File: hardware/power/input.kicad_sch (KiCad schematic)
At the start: 26 parts, among them J101 24V IN, Q101 SQJ457EP, Q102 SQJ457EP, SW101 POWER, U101 L78M05, U102 74HC14

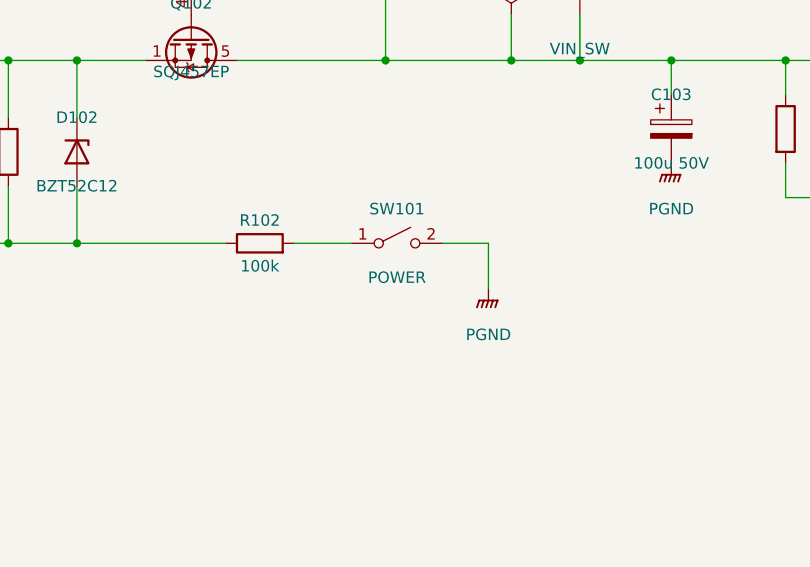
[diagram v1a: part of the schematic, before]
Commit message: Power board: E24 dividers, rear-panel rocker, last parts chosen (decisions 156-159)
- 156: UVLO 680k/39k (start 21.3 V, stop 19.0 V), RT 240k, buck
  compensation 16k; design.py and startup_sim.py rerun (start-up unchanged,
  GSM220B24 limit in the model)
- 157: power switch a Legion SS11-BBIWG-R20-R rocker on the rear panel,
  wired to J102 (JST XH 2-pin) in place of SW101; counted in costs.py
- 158: C103 Nichicon UHE1H101MPD radial; sync caps 10 pF C0G 50 V 0603
- 159: D201 SS54 on D_SMA to match LCSC C22452
- Netlist checks 0 problems, ERC 0/0; estimate 764/1045/1641 EUR
  (4/8/16 ch), 28 fee types

Co-Authored-By: Claude Opus 5.5 <noreply@anthropic.com>
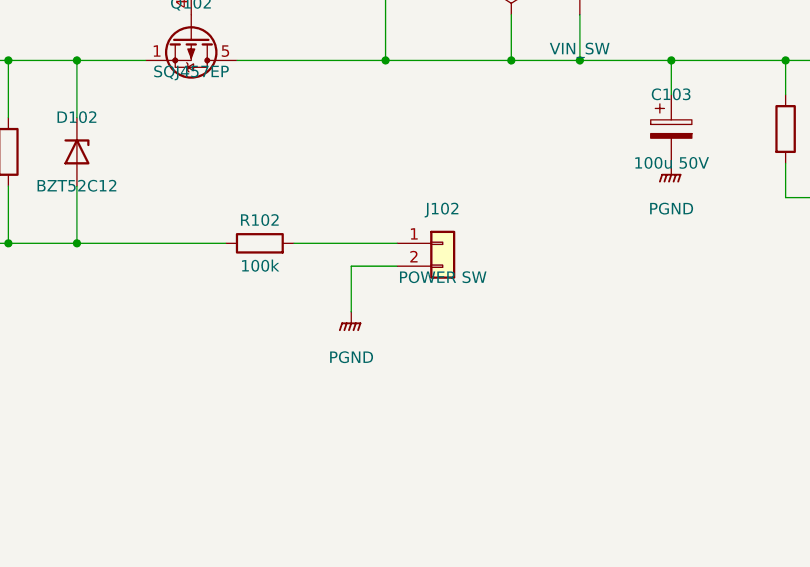
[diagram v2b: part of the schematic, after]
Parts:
- removed SW101: POWER, symbol Switch:SW_SPST
- added J102: POWER SW, Connector_JST:JST_XH_B2B-XH-A_1x02_P2.50mm_Vertical, symbol Connector_Generic:Conn_01x02
- C103: footprint Capacitor_SMD:CP_Elec_8x10.5 -> Capacitor_THT:CP_Radial_D8.0mm_P3.50mm; MPN (none) -> UHE1H101MPD; Manufacturer (none) -> Nichicon; ProjectPN SX-C-021 -> SX-C-028; Supplier (none) -> LCSC; SupplierPN (none) -> C116229
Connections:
- net PGND: now also J102.2 (Pin_2)
- net at R102.2: now also J102.1 (Pin_1)

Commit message: Power: power LED on the power bay's top strip (decision 168)
The power board stands on edge in the bay (decision 162), so the
on-board 0805 power LED could not be seen. D103 leaves the board;
R104 feeds a JST XH 2-pin header J103 wired to a 3 mm Kingbright
WP710A10LGD (SX-D-004) in a Bivar CR-104 clip (SX-MECH-006, new) on
the bay's top strip. Both off-board parts are costed with the frame,
like the rocker. Netlist checks 0 problems, ERC 0/0.

Co-Authored-By: Claude Opus 5.5 <noreply@anthropic.com>
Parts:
- removed D103: POWER, LED_SMD:LED_0805_2012Metric, symbol Device:LED
- added J103: POWER LED, Connector_JST:JST_XH_B2B-XH-A_1x02_P2.50mm_Vertical, symbol Connector_Generic:Conn_01x02
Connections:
- net PGND: now also J103.2 (Pin_2)
- net at R104.2: now also J103.1 (Pin_1)

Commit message: Power board: PCB placed and routed by scripts, panel-mount brick jack, small module without chain 2 (decisions 182, 185, 186)
Co-Authored-By: Claude Opus 5.5 <noreply@anthropic.com>
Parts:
- J101: footprint (none) -> Connector_JST:JST_VH_B4P-VH_1x04_P3.96mm_Vertical; MPN KPJX-4S -> B4P-VH(LF)(SN); Manufacturer Kycon -> JST; Note Locking 4-pin power DIN, PCB right angle at the rear edge; 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 -> Brick jack lead: Kycon KPJX-PM-4S panel jack (SX-CONN-027) 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; ProjectPN SX-CONN-011 -> SX-CONN-026; Supplier DigiKey -> LCSC; SupplierPN (none) -> C160317
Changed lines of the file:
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@@
 			)
 		)
-		(property "Footprint" ""
+		(property "Footprint" "Connector_JST:JST_VH_B4P-VH_1x04_P3.96mm_Vertical"
 			(at 40.64 101.6 180)
 			(hide yes)
@@
 			)
 		)
-		(property "ProjectPN" "SX-CONN-011"
+		(property "ProjectPN" "SX-CONN-026"
 			(at 40.64 101.6 0)
 			(hide yes)
@@
 			)
 		)
-		(property "Manufacturer" "Kycon"
+		(property "Manufacturer" "JST"
 			(at 40.64 101.6 0)
 			(hide yes)
@@
 			)
 		)
-		(property "MPN" "KPJX-4S"
+		(property "MPN" "B4P-VH(LF)(SN)"
 			(at 40.64 101.6 0)
 			(hide yes)
@@
 			)
 		)
-		(property "Supplier" "DigiKey"
+		(property "Supplier" "LCSC"
 			(at 40.64 101.6 0)
 			(hide yes)
@@
 			)
 		)
-		(property "SupplierPN" ""
+		(property "SupplierPN" "C160317"
 			(at 40.64 101.6 0)
 			(hide yes)
@@
 			)
 		)
-		(property "Note" "Locking 4-pin power DIN, PCB right angle at the rear edge; mates Mean Well R7B (KPPX-4P). Check polarity on the first brick"
+		(property "Note" "Brick jack lead: Kycon KPJX-PM-4S panel jack (SX-CONN-027) on the bay's rear strip, four 18 AWG wires, pin n to jack pin n (1, 4 = +24 V; 2, 3 = 0 V); VHR-4N housing with SVH-21T-P1.1 contacts (decision 182). Check polarity on the first brick"
 			(at 40.64 101.6 0)
 			(hide yes)

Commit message: Power board: input EMI pi filter C108/L101 after Q102, PCB rebuilt (decision 187)
C108 4.7 uF 100 V on the brick side, L101 2.2 uH SRP7028A in series, then C103:
keeps the converters' 400 kHz input current off the brick lead (about -80 dB
against -44 dB in a hand model; L101 alone gains nothing because C101 resonates
with the lead near 400 kHz). No new part type. Input area re-placed (F101
upright, Q101/Q102 to the rear, VIN_PRE copper under L101); placement.py now
takes new parts and pad nets from the schematic. ERC 0/0, DRC 0, parity clean.

Co-Authored-By: Claude Opus 5.5 <noreply@anthropic.com>
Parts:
- added C108: 4u7 100V, Capacitor_SMD:C_1210_3225Metric, symbol Device:C
- added L101: 2u2, Inductor_SMD:L_Bourns_SRP7028A_7.3x6.6mm, symbol Device:L
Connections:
- net PGND: now also C108.2
- net VIN_SW: now also L101.2; no longer C102.2, Q102.5 (D)
- new net VIN_PRE: C102.2, C108.1, L101.1, Q102.5 (D)
